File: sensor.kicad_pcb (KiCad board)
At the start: 2 copper layers, 62 x 65 mm, 91 parts, among them CON1 Micro USB, CON2 PROG, CON3 Jack-DC, CON4 HTU21D, CON5 Conn_01x08, Q1 BSS214N, Q2 BSS214N, Q3 BSS214N, Q4 BSS214N, Q5 BSS214N, Q6 BSS214N, SW1 RESET, SW2 CFG, U1 LM7805, U2 TLV1117LV33DCY, U3 ESP-12F, U4 HTU21D, U5 PMS7003

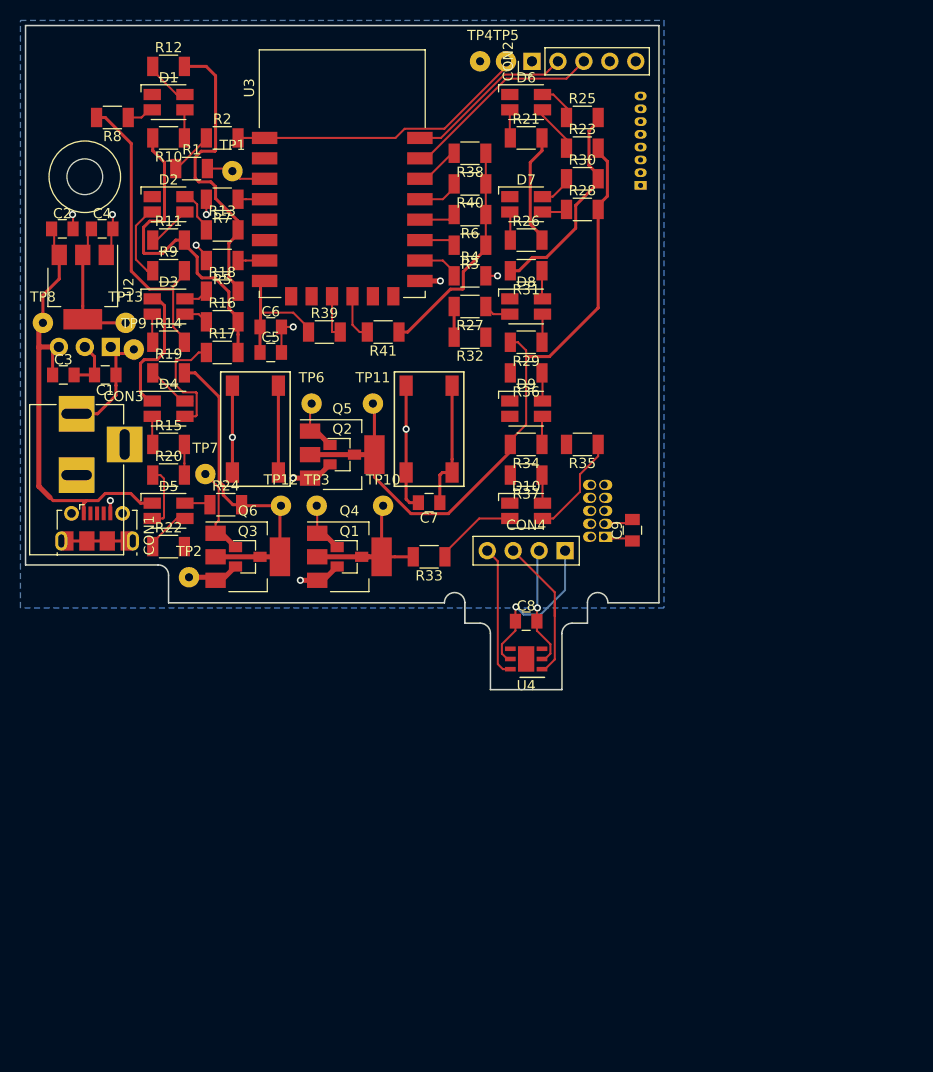
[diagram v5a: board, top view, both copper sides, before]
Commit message: Routed PCB, routing to be optimized
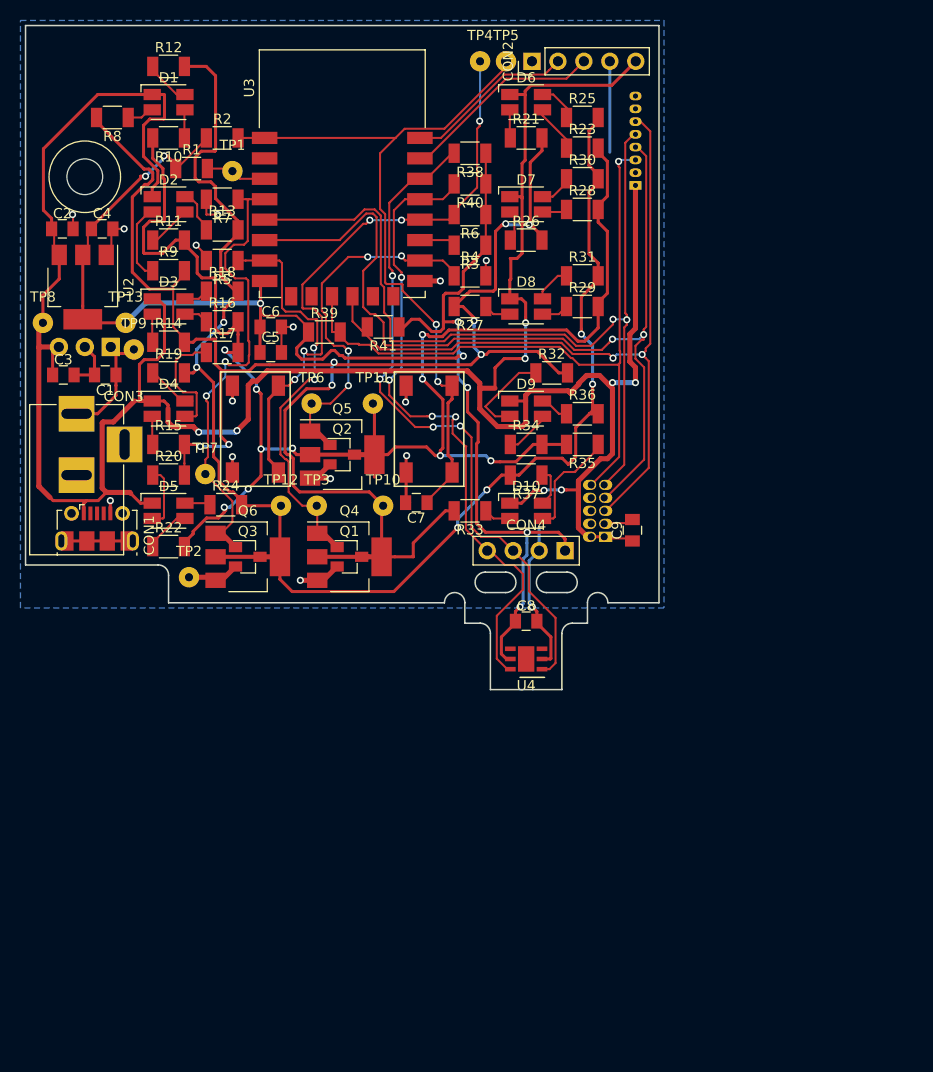
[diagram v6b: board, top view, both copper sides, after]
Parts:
- moved R32 8.73 mm to (117.5, 75.5), turned to 0 degrees
- moved R36 6.80 mm to (120.5, 79.5), turned to 0 degrees
- moved R29 6.52 mm to (120.5, 69.0), turned to 0 degrees
- moved R33 6.02 mm to (109.5, 89.0)
- moved R31 5.52 mm to (120.5, 66.0), turned to 0 degrees
- moved C7 1.25 mm to (104.2, 88.2)
- moved CON5 0.50 mm to (125.7, 57.1)
- moved R41 0.50 mm to (101.0, 71.0)
- turned R34 to 0 degrees
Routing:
- net +5V: track 61.9 -> 270.6 mm, vias 0 -> 8
- net /LED_R: track 62.3 -> 168.7 mm, vias 0 -> 8
- net PMS_RXD: track 0.00 -> 90.6 mm, vias 0 -> 2
- net PMS_TXD: track 0.00 -> 85.8 mm, vias 0 -> 2
- net +3V3: track 72.0 -> 152.3 mm, vias 1 -> 8
- net PMS_RESET: track 4.54 -> 74.7 mm, vias 0 -> 2
- net /LED_B: track 81.5 -> 147.4 mm, vias 0 -> 6
- net PMS_SET: track 4.27 -> 69.1 mm, vias 0 -> 1
- net /LED_G: track 100.5 -> 151.6 mm, vias 0 -> 10
- net HTU_SDA: track 19.9 -> 66.5 mm, vias 0 -> 4
- net HTU_SCL: track 17.2 -> 63.7 mm, vias 0 -> 4
- net CFG_BTN: track 12.1 -> 58.1 mm, vias 0 -> 5
- net LED_B_CTRL: track 11.6 -> 46.7 mm, vias 0 -> 2
- net LED_R_CTRL: track 7.83 -> 40.5 mm, vias 0 -> 2
- net RESET: track 42.2 -> 71.7 mm, vias 0 -> 2
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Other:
- outline, holes or cut-outs redrawn

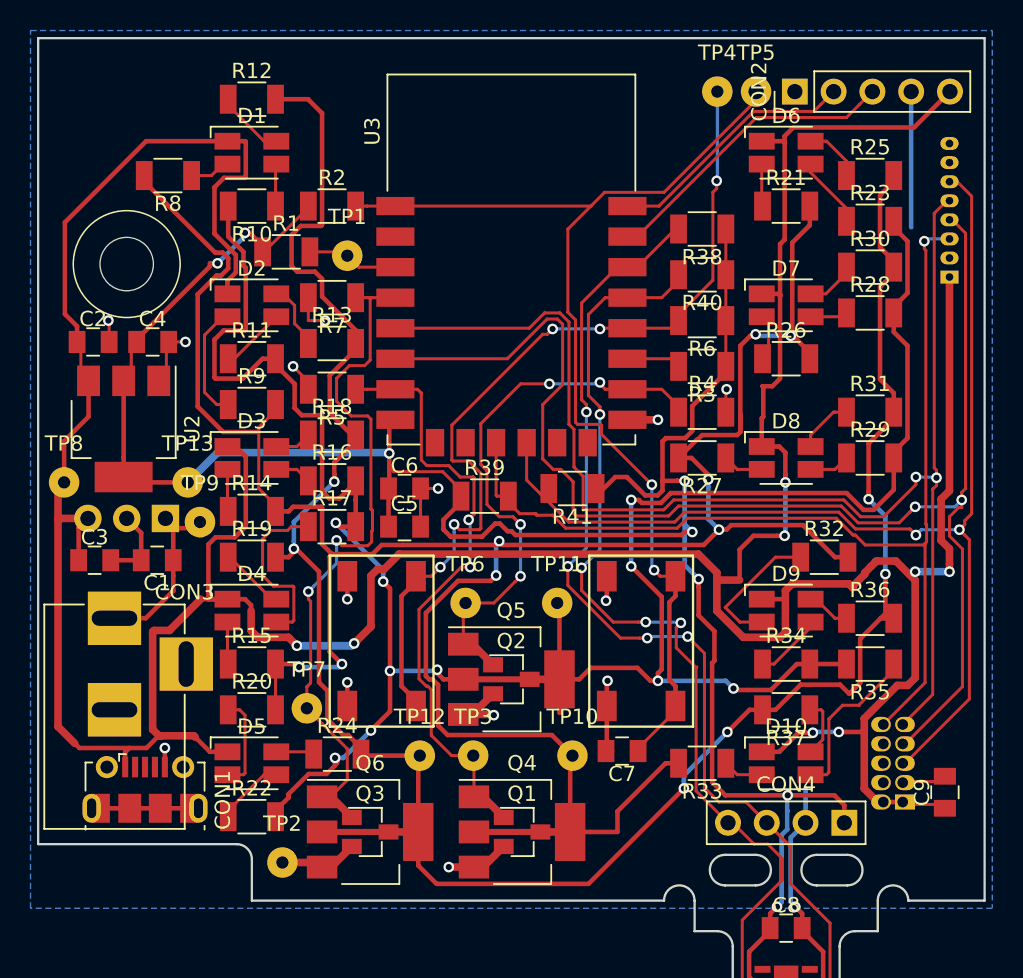
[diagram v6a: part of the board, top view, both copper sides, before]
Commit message: Change some footprints. Optimize routing.
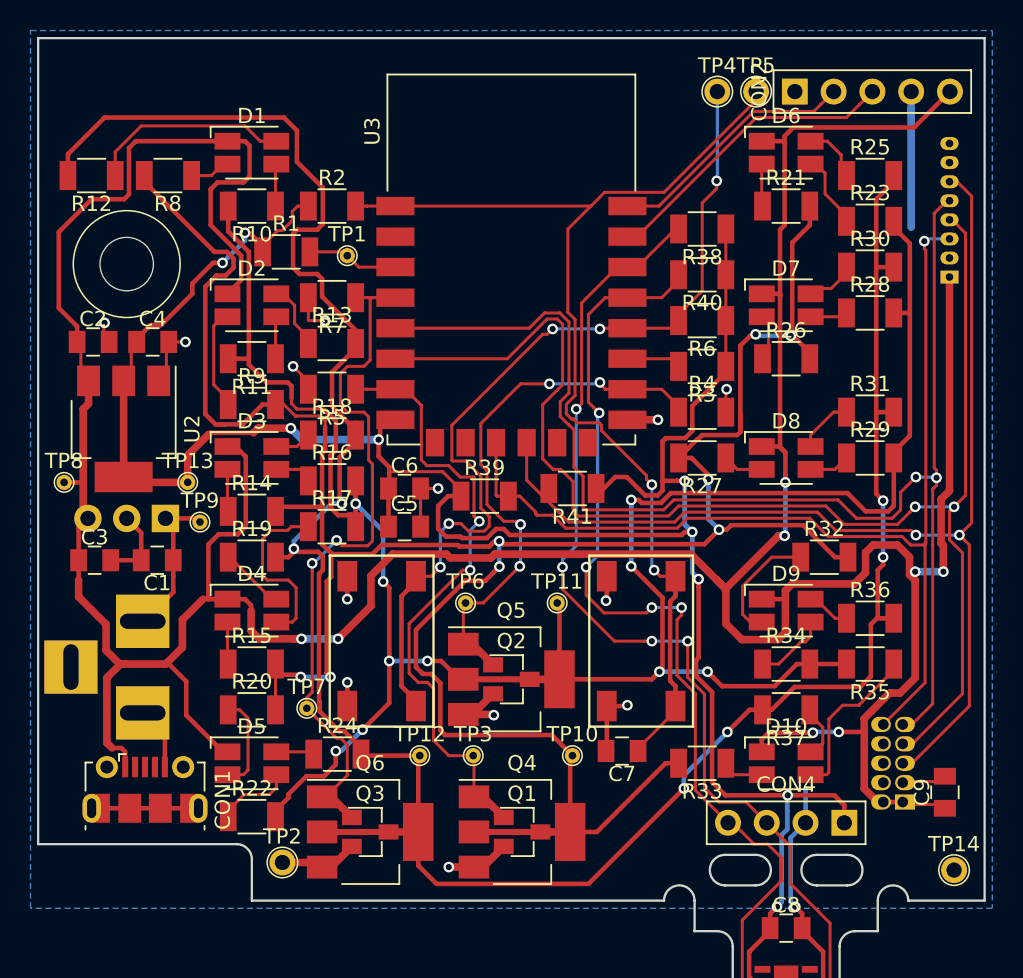
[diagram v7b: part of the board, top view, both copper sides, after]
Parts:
- added TP14: GND, less-smog:TP_1.7_1.0_THT, F.Cu at (126.0, 96.0)
- CON2: footprint Pin_Headers:Pin_Header_Straight_1x05_Pitch2.54mm -> less-smog:Pin_Header_Straight_1x05_Pitch2.54mm
- CON3: moved to B.Cu
- TP1, TP10, TP11, TP12, TP13, TP3, TP6, TP7, TP8, TP9: footprint Wire_Pads:SolderWirePad_single_0-8mmDrill -> less-smog:TP_1.0_0.5_THT
- TP2, TP4, TP5: footprint Wire_Pads:SolderWirePad_single_0-8mmDrill -> less-smog:TP_1.7_1.0_THT
- moved R12 11.6 mm to (69.5, 50.5), turned to 180 degrees
- moved CON3 1.86 mm to (72.8, 79.7)
- turned R11 to 180 degrees
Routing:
- net /LED_B: track 147.4 -> 162.6 mm
- net Net-(D1-Pad2): track 4.59 -> 14.1 mm
- net +5V: track 270.6 -> 263.6 mm
- net /LED_R: track 168.7 -> 173.3 mm
- net +3V3: track 152.3 -> 156.1 mm, vias 8 -> 9
- net /LED_G: track 151.6 -> 148.5 mm
- net GND: track 79.4 -> 82.3 mm, vias 15 -> 14
- net +12V: track 12.4 -> 10.2 mm
- net Net-(D2-Pad3): track 4.29 -> 2.77 mm
- net PMS_TXD: track 85.8 -> 87.1 mm
- net Net-(D9-Pad4): track 9.09 -> 7.89 mm
- net CFG_BTN: track 58.1 -> 59.1 mm
- net Net-(D2-Pad4): track 7.63 -> 6.69 mm
- net HTU_SCL: track 63.7 -> 64.3 mm
- net LED_R_CTRL: track 40.5 -> 41.0 mm
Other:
- net class Power: trace_width 0.3 -> 0.2
